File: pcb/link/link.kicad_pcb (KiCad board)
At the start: 8 copper layers, 153.7 x 88.9 mm, 382 parts, among them IC1 IS31FL3236A-TQLS4-TR, J1 STLINK-V3MINIE, J10 3-2328724-1, J11 68021-204HLF, J13 68021-204HLF, J14 68021-204HLF, J16 68021-204HLF, J18 68021-204HLF, J19 USB4105-GF-A, J2 MEM2061-01-188-00-A, J3 SACC-DSIV-M12MS-5CON-L180, J4 68021-204HLF, J5 68021-204HLF, J6 FFC2B35-10-T, J7 USB4105-GF-A, J8 ARJM11B1-009-AB-EW2, J9 ARJM11B1-009-AB-EW2, Q1 PMV20ENR, Q2 PMV20ENR, Q3 PMV20ENR, SW1 TL6400AF160QJ, U1 STM32F479VGT6, U10 TPS2021D, U11 TPS2021D, U12 LM1085ISX-3.3/NOPB, U13 INA226AIDGSR, U14 NC7SZ86P5X, U2 CAHCT1G14QDBVRQ1, U3 TS3DV416DGGR, U4 W5500, U5 W5500, U6 USB3340-EZK-TR, U7 ADG772BCPZ-1REEL, U8 TPS6734ID, U9 LTC4415EMSE#TRPBF, Y1 ECS-2520SMV-240-FP-TR, Y2 ECS-2520SMV-240-FP-TR, Y3 ECS-TXO-2520MV-250-AN-TR, Y4 ECS-TXO-2520MV-250-AN-TR

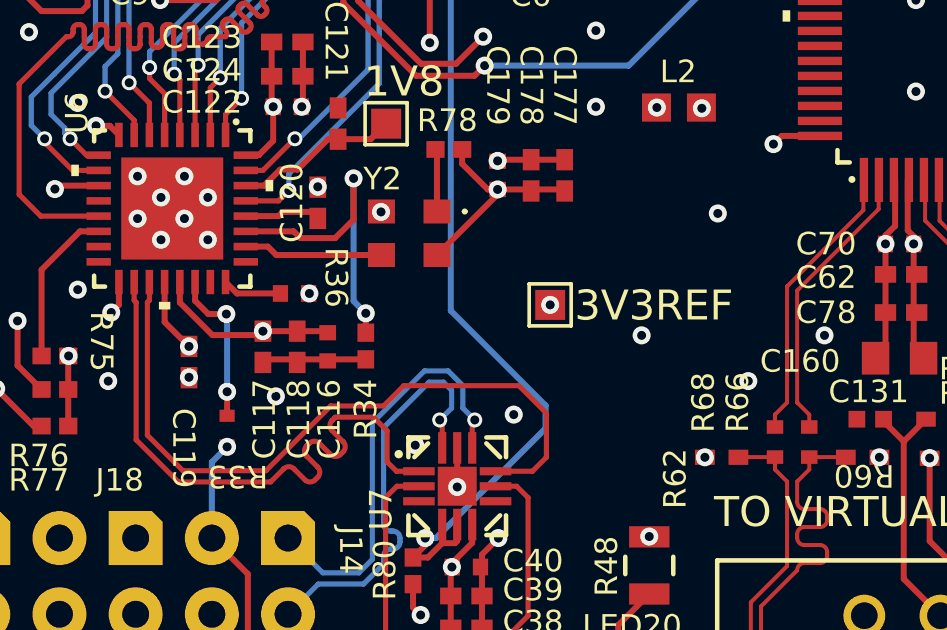
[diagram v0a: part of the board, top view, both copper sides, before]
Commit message: remove 3V3VREF TP (and upgrade to kicad 10) (closes #105)
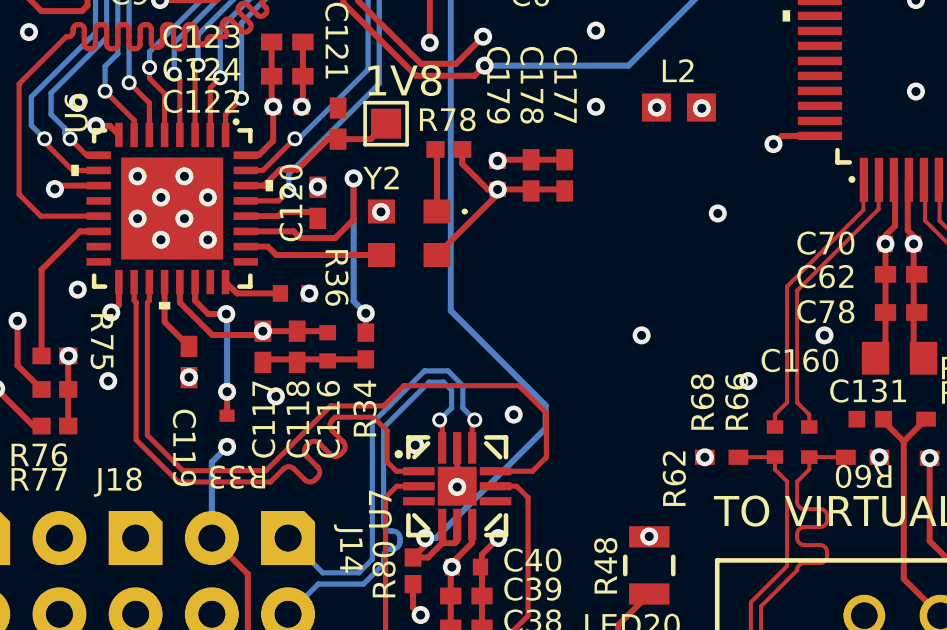
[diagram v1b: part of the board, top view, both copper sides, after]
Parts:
- removed TP5: 3.3V ULPI, TestPoint:TestPoint_Pad_1.0x1.0mm
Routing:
- net Net-(U6-VDD33): track 15.4 -> 2.48 mm, vias 2 -> 0
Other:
- board text removed: "3V3REF"
